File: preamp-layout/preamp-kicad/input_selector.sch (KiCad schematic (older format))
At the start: 45 parts, among them J35 Conn_01x03_Male, J36 Conn_01x03_Male, J37 Conn_01x03_Male, J38 Conn_01x03_Male, J39 Conn_01x03_Male, J40 Conn_01x03_Male, J41 Conn_01x03_Male, J42 Conn_01x03_Female, J43 Conn_01x03_Female, J44 Conn_01x02_Female, J45 Conn_01x07_Female, J46 Conn_01x07_Female, J47 Conn_01x02_Male, J48 Conn_01x02_Male, K2 G6JU, K3 G6JU, K4 G6JU, K5 G6JU, K6 G6JU, K7 G6JU, K8 G6JU, U10 ULN2003, U8 MCP23017_SO, U9 ULN2003

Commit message: Periodic backup
Extensive changes as a result of PCB layout phase.
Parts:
- removed J35, J36, J37, J38, J39, J40, J41: Conn_01x03_Male, Connector_PinHeader_2.54mm:PinHeader_1x03_P2.54mm_Vertical, symbol Connector:Conn_01x03_Male
- removed J45, J46: Conn_01x07_Female, Connector_PinHeader_2.54mm:PinHeader_1x07_P2.54mm_Vertical, symbol Connector:Conn_01x07_Female
- removed K3, K4, K5, K6: G6JU, preamp:Relay_DPDT_Omron_G6JU-2P-Y, symbol preamp:G6JU
- removed U10, U9: ULN2003, Package_SO:SOIC-16_3.9x9.9mm_P1.27mm, symbol Transistor_Array:ULN2003
- added C123, C92, C93: 0.1uF, Capacitor_SMD:C_0805_2012Metric_Pad1.15x1.40mm_HandSolder, symbol Device:C
- added D61, D62: GREEN, LED_SMD:LED_1206_3216Metric_Pad1.42x1.75mm_HandSolder, symbol Device:LED
- added J26: Conn_01x18_Male, Connector_PinHeader_2.54mm:PinHeader_1x18_P2.54mm_Vertical, symbol Connector:Conn_01x18_Male
- added J27: Conn_01x08_Male, Connector_PinHeader_2.54mm:PinHeader_1x08_P2.54mm_Vertical, symbol Connector:Conn_01x08_Male
- added J30: Conn_01x04_Female, Connector_PinSocket_2.54mm:PinSocket_1x04_P2.54mm_Vertical, symbol Connector:Conn_01x04_Female
- added J95, J96: Conn_01x03_Male, Connector_JST:JST_EH_S3B-EH_1x03_P2.50mm_Horizontal, symbol Connector:Conn_01x03_Male
- added R139, R140, R141, R142, R143, R144, R145, R146, R147, R148: 100R, Resistor_SMD:R_1206_3216Metric_Pad1.42x1.75mm_HandSolder, symbol Device:R
- added U10, U9: DG408DY, Package_SO:SOIC-16_3.9x9.9mm_P1.27mm, symbol preamp:DG408DY
- added U24: ULN2003, Package_SO:SOIC-16_3.9x9.9mm_P1.27mm, symbol Transistor_Array:ULN2003
- J42, J43: footprint Connector_PinHeader_2.54mm:PinHeader_1x03_P2.54mm_Vertical -> Connector_PinSocket_2.54mm:PinSocket_1x03_P2.54mm_Vertical
- J44: footprint Connector_PinHeader_2.54mm:PinHeader_1x02_P2.54mm_Vertical -> Connector_JST:JST_EH_S2B-EH_1x02_P2.50mm_Horizontal
- J47, J48: footprint Connector_JST:JST_EH_B2B-EH-A_1x02_P2.50mm_Vertical -> Connector_JST:JST_EH_S2B-EH_1x02_P2.50mm_Horizontal
- R24, R25: value 51R -> 1.5k
- R28, R29, R30, R31, R32, R33: value 51R -> 100R
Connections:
- net IN_3_R+ is gone; now on net A_IN_2_L: R29.2
- net IN_3_S+ is gone; now on net A_IN_1_L: R28.2
- net IN_4_R+ is gone; now on net A_IN_4_L: R31.2
- net IN_4_S+ is gone; now on net A_IN_3_L: R30.2
- net IN_5_S+ is gone; now on net A_IN_5_L: R32.2
- net +5V: now also C123.1, J30.3 (Pin_3), U24.9 (COM); no longer C19.1, C20.1, R24.1, R25.1, R28.1, R29.1, R30.1, R31.1, R32.1, R33.1
- net A_IN_1_L: now also J26.2 (Pin_2); no longer K2.3
- net A_IN_1_R: now also J26.3 (Pin_3), R141.2; no longer K2.6
- net A_IN_2_L: now also J26.4 (Pin_4)
- net A_IN_2_R: now also J26.5 (Pin_5), R142.2
- net A_IN_3_L: now also J26.6 (Pin_6)
- net A_IN_3_R: now also J26.7 (Pin_7), R143.2
- net A_IN_4_L: now also J26.8 (Pin_8)
- net A_IN_4_R: now also J26.9 (Pin_9), R144.2
- net A_IN_5_L: now also J26.10 (Pin_10)
- net A_IN_5_R: now also J26.11 (Pin_11), R145.2
- net A_IN_L: now also K2.4
- net A_IN_R: now also K2.5
- net A_OUT_1_L: now also J27.2 (Pin_2)
- net A_OUT_1_R: now also J27.3 (Pin_3)
- net A_OUT_2_L: now also J27.4 (Pin_4)
- net A_OUT_2_R: now also J27.5 (Pin_5)
- net A_OUT_L: now also U10.8 (D); no longer K2.4
- net A_OUT_R: now also U9.8 (D); no longer K2.5
- net GND: now also K2.2, K2.7, C123.2, C92.2, C93.2, D61.1 (K), D62.2 (A), J26.1 (Pin_1), J26.18 (Pin_18), J27.1 (Pin_1), J27.8 (Pin_8), J30.4 (Pin_4), J95.2 (Pin_2), J96.2 (Pin_2), U10.14 (GND), U24.8 (GND), U9.14 (GND)
- net OUT_1_R+: now also U24.15 (O2)
- net OUT_1_S+: now also U24.16 (O1)
- net OUT_2_R+: now also U24.13 (O4)
- net OUT_2_S+: now also U24.14 (O3)
- net IN_L_SEL_A0: now reaches U8.1 (GPB0)
- net IN_L_SEL_A0: now also U10.1 (A0)
- net IN_L_SEL_A1: now reaches U8.2 (GPB1)
- net IN_L_SEL_A1: now also U10.16 (A1)
- net IN_L_SEL_A2: now reaches U8.3 (GPB2)
- net IN_L_SEL_A2: now also U10.15 (A2)
- net IN_R_SEL_A0: now reaches U8.4 (GPB3)
- net IN_R_SEL_A0: now also U9.1 (A0)
- net IN_R_SEL_A1: now reaches U8.5 (GPB4)
- net IN_R_SEL_A1: now also U9.16 (A1)
- net IN_R_SEL_A2: now reaches U8.6 (GPB5)
- net IN_R_SEL_A2: now also U9.15 (A2)
- net at U8.25 (GPA4): now also U24.1 (I1)
- net at U8.26 (GPA5): now also U24.2 (I2)
- net at U8.27 (GPA6): now also U24.3 (I3)
- net at U8.28 (GPA7): now also U24.4 (I4)
- net IN_1_R+: no longer names the net of R25.2
- net IN_1_R+: now also D62.1 (K); no longer K2.8
- net IN_1_S+: no longer names the net of R24.2
- net IN_1_S+: now also D61.2 (A); no longer K2.1
- net IN_2_R+ renamed OUT_3_R+
- net OUT_3_R+: now also K2.8, U24.11 (O6)
- net IN_2_S+ renamed OUT_3_S+
- net OUT_3_S+: now also K2.1, U24.12 (O5)
- net IN_5_R+ renamed A_IN_6_L
- net A_IN_6_L: now also J26.12 (Pin_12)
- new net: R139.1, U10.10 (S7)
- new net: R33.1, U10.11 (S6)
- new net: R32.1, U10.12 (S5)
- new net: R28.1, U10.4 (S1)
- new net: R29.1, U10.5 (S2)
- new net: R30.1, U10.6 (S3)
- new net: R31.1, U10.7 (S4)
- new net: R140.1, U10.9 (S8)
- new net: R147.1, U9.10 (S7)
- new net: R146.1, U9.11 (S6)
- new net: R145.1, U9.12 (S5)
- new net: R141.1, U9.4 (S1)
- new net: R142.1, U9.5 (S2)
- new net: R143.1, U9.6 (S3)
- new net: R144.1, U9.7 (S4)
- new net: R148.1, U9.9 (S8)
- new net +15V: C19.1, C20.1, J30.1 (Pin_1), J95.1 (Pin_1), J96.1 (Pin_1), R24.1, U10.13 (V+), U10.2 (EN), U9.13 (V+), U9.2 (EN)
- new net -15V: C92.1, C93.1, J30.2 (Pin_2), J95.3 (Pin_3), J96.3 (Pin_3), R25.1, U10.3 (V-), U9.3 (V-)
- new net A_IN_6_R: J26.13 (Pin_13), R146.2
- new net A_IN_7_L: J26.14 (Pin_14), R139.2
- new net A_IN_7_R: J26.15 (Pin_15), R147.2
- new net A_IN_8_L: J26.16 (Pin_16), R140.2
- new net A_IN_8_R: J26.17 (Pin_17), R148.2
- new net A_OUT_3_L: J27.6 (Pin_6), K2.3
- new net A_OUT_3_R: J27.7 (Pin_7), K2.6
- no-connect marks 14 -> 12
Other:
- note added: "8x 100R"
- note added: "OUT 3"
- note removed: "IN 1"
- note removed: "IN 2"
- note removed: "IN 3"
- note removed: "IN 4"
- note removed: "IN 5"
- moved on the sheet: C19, C20, C21, D12, J42, J43, J44, J47, J48, K7A, K7B, K7C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

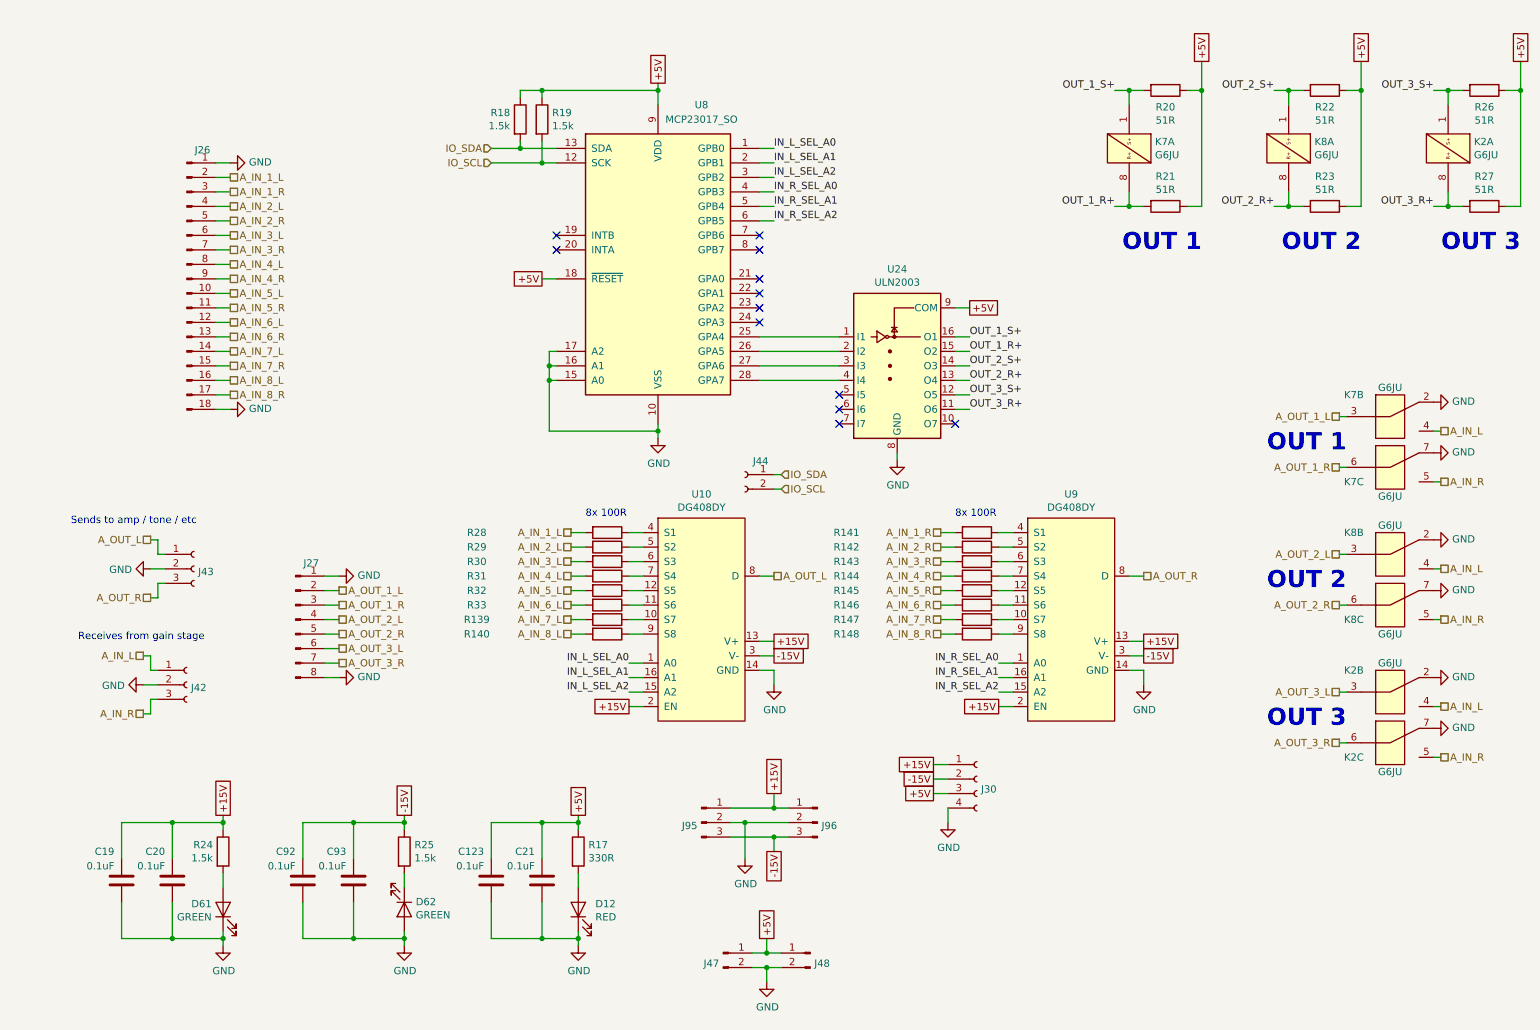
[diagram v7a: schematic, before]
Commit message: PCB layout
trying a different layout for the gain stage board, this serves as a reference point.
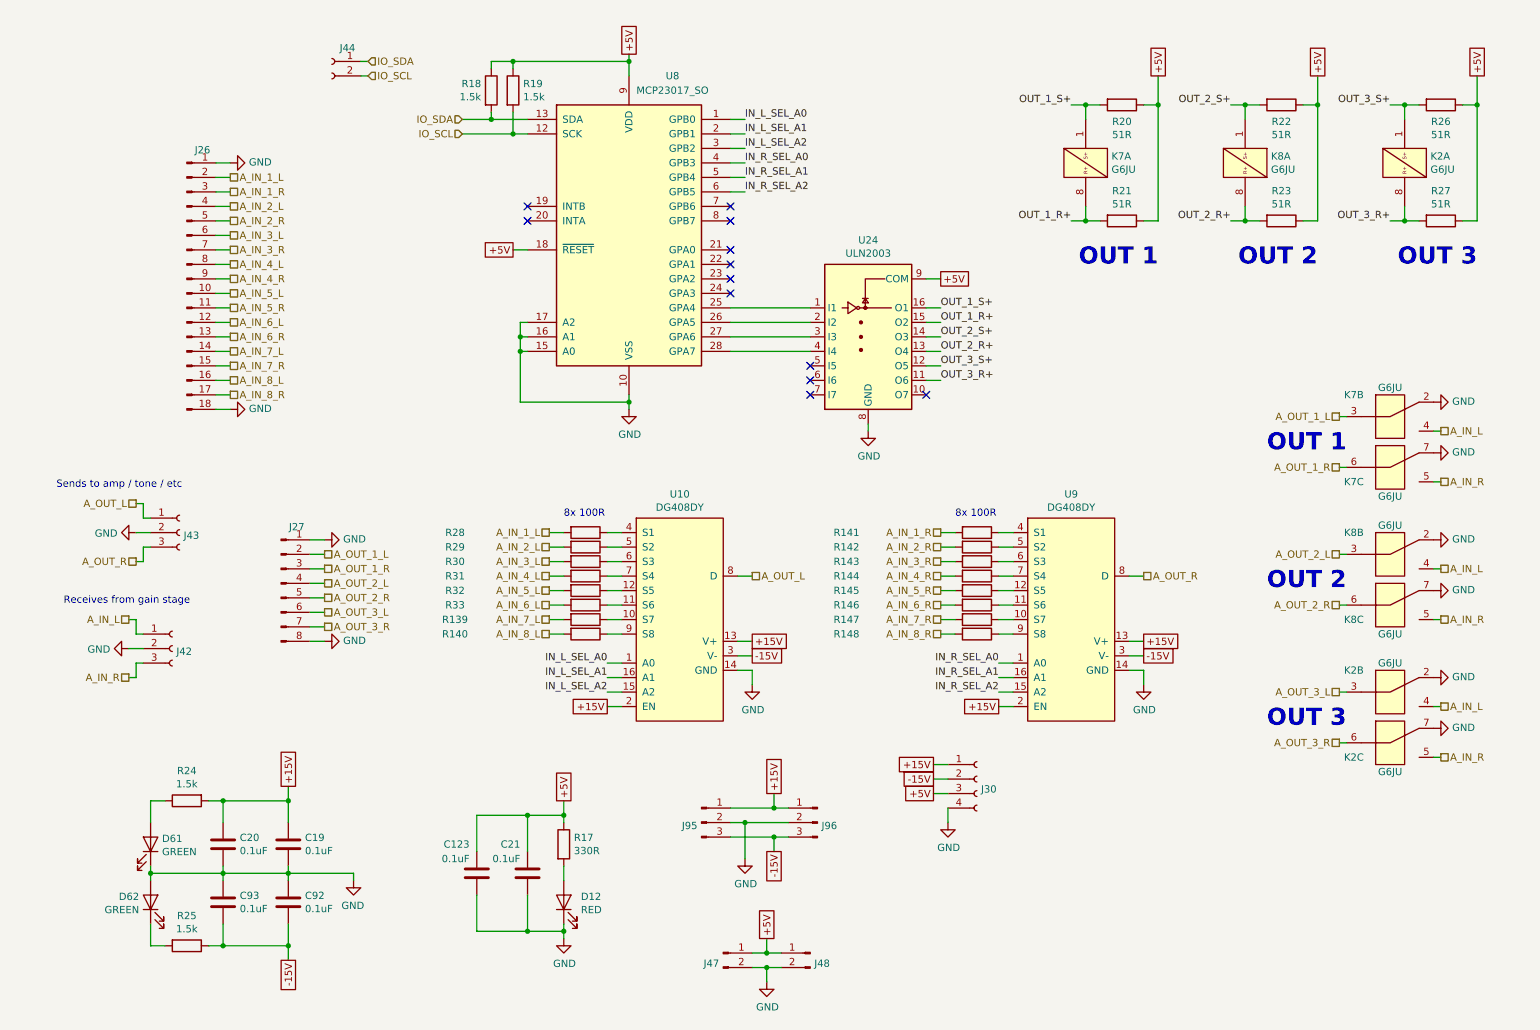
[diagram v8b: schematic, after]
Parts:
- C123, C19, C20, C21, C92, C93: footprint Capacitor_SMD:C_0805_2012Metric_Pad1.15x1.40mm_HandSolder -> Capacitor_SMD:C_1206_3216Metric_Pad1.42x1.75mm_HandSolder
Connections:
- net +15V: now also R24.2; no longer R24.1
- net at D61.2 (A): now also R24.1; no longer R24.2
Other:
- moved on the sheet: C123, C19, C20, C21, C92, C93, D12, D61, D62, J27, J42, J43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
